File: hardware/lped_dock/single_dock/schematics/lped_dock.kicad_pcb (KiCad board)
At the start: 2 copper layers, 25 x 16 mm, 18 parts, among them J1 V_{OUT}, J2 CONN, J3 GND, J7 USB-C connector, U1 TPD4E02B04DQA, U2 TPS560200

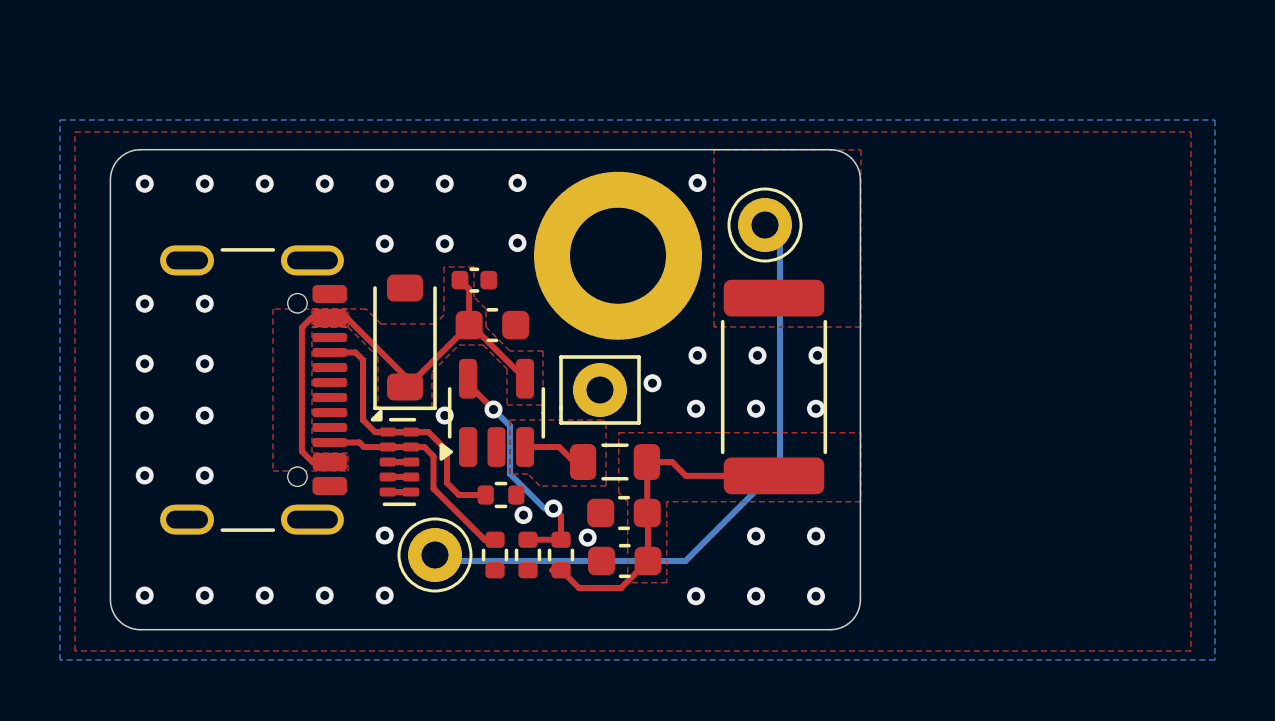
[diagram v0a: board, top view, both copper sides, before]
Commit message: feat(hardware): add battery charger and connector to single charger
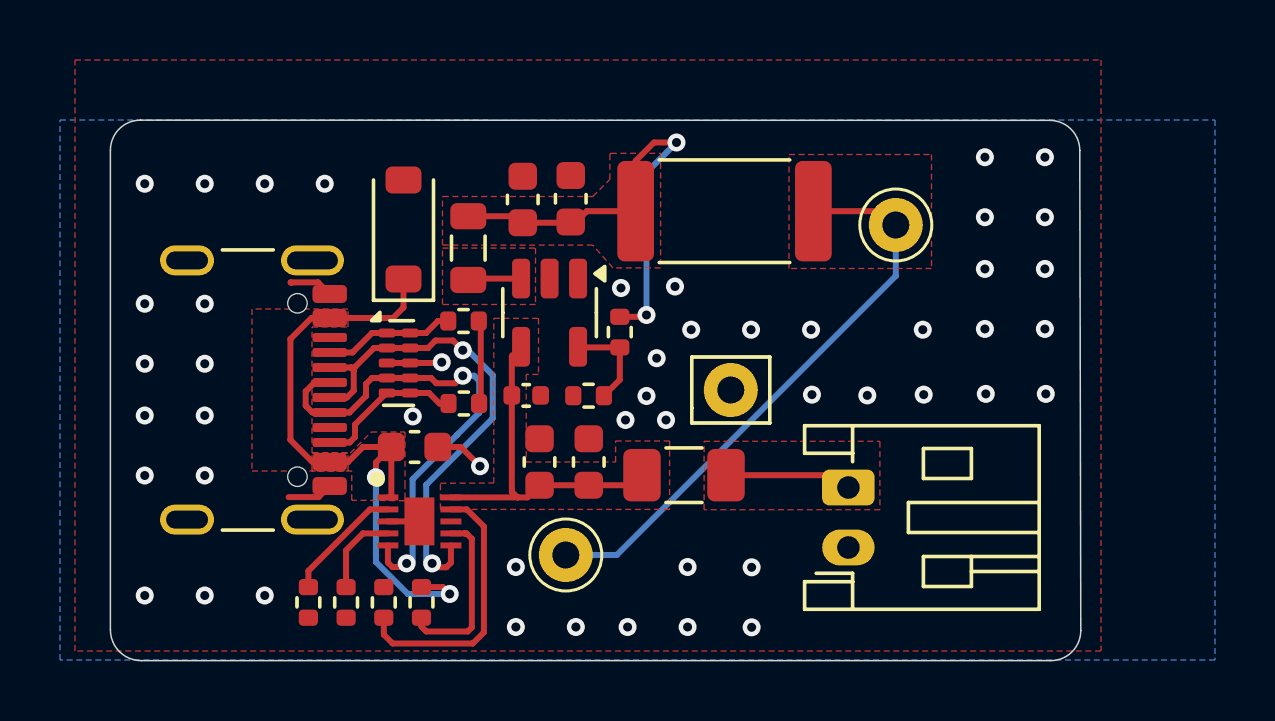
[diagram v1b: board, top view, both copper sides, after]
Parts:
- removed H1: M3, MountingHole:MountingHole_3.2mm_M3_DIN965_Pad
- added BT1: Battery_Cell, Connector_JST:JST_PH_S2B-PH-K_1x02_P2.00mm_Horizontal, F.Cu at (127.3, 112.2)
- added C5: 1u, Capacitor_SMD:C_0603_1608Metric, F.Cu at (112.8, 108.9)
- added C6: 1u, Capacitor_SMD:C_0603_1608Metric, F.Cu at (117.0, 109.4)
- added F1: Polyfuse_Small, Fuse:Fuse_1206_3216Metric, F.Cu at (121.8, 109.8)
- added IC1: BQ24050DSQR, Battery_Chargers:SON40P200X200X80-11N, F.Cu at (113.0, 111.4)
- added R1: 2k7, Resistor_SMD:R_0402_1005Metric, F.Cu at (109.3, 114.1)
- added R7: 10k, Resistor_SMD:R_0402_1005Metric, F.Cu at (113.0, 114.1)
- added R8: 2k, Resistor_SMD:R_0402_1005Metric, F.Cu at (110.5, 114.1)
- added TH1: 10k, Resistor_SMD:R_0402_1005Metric, F.Cu at (111.8, 114.1)
- moved C2 12.5 mm to (116.4, 100.7), turned to 90 degrees
- moved C1 10.6 mm to (118.0, 100.6), turned to 90 degrees
- moved L1 8.65 mm to (114.6, 102.3), turned to 90 degrees
- moved R3 7.68 mm to (119.7, 105.1), turned to -90 degrees
- moved R2 6.09 mm to (123.2, 101.0), turned to 0 degrees
- moved R5 5.93 mm to (114.5, 104.7)
- moved R4 5.68 mm to (118.6, 107.2), turned to 180 degrees
- moved C3 5.58 mm to (118.6, 109.4), turned to 90 degrees
- moved R6 5.16 mm to (114.5, 107.5), turned to 0 degrees
- moved J1 4.36 mm to (128.9, 101.5)
- moved J2 4.36 mm to (117.9, 112.5)
- moved J3 4.36 mm to (123.4, 107.0)
- moved C4 4.21 mm to (116.5, 107.2)
- moved U2 3.78 mm to (117.3, 104.4), turned to -90 degrees
- moved D3 3.60 mm to (112.5, 101.7)
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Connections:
- C3 pad 1: /Regulator/V_{IN} -> /Battery Charger/V_{SYS}
- C4 pad 1: /Regulator/V_{IN} -> /Battery Charger/V_{SYS}
- D3 pad 1: /Regulator/V_{IN} -> /Battery Charger/V_{BUS}
- J7 pad A4: /Regulator/V_{IN} -> /Battery Charger/V_{BUS}
- J7 pad A6: unconnected-(J7-D+-PadA6) -> /USB/USB_D+
- J7 pad A7: unconnected-(J7-D--PadA7) -> /USB/USB_D-
- J7 pad A9: /Regulator/V_{IN} -> /Battery Charger/V_{BUS}
- J7 pad B4: /Regulator/V_{IN} -> /Battery Charger/V_{BUS}
- J7 pad B6: unconnected-(J7-D+-PadB6) -> /USB/USB_D+
- J7 pad B7: unconnected-(J7-D--PadB7) -> /USB/USB_D-
- J7 pad B9: /Regulator/V_{IN} -> /Battery Charger/V_{BUS}
- U1 pad 2: /USB/CC2 -> /USB/USB_D-
- U1 pad 4: /USB/D- -> /USB/USB_D+
- U1 pad 5: /USB/D+ -> /USB/CC2
- U1 pad 6: /USB/D+ -> /USB/CC2
- U1 pad 7: /USB/D- -> /USB/USB_D+
- U1 pad 9: /USB/CC2 -> /USB/USB_D-
- U2 pad 4: /Regulator/V_{IN} -> /Battery Charger/V_{SYS}
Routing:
- net /Battery Charger/V_{BUS}: track 0.00 -> 22.1 mm, vias 0 -> 2
- net /Regulator/V_{IN}: track 16.9 -> 0.00 mm
- net /USB/USB_D+: track 0.00 -> 16.7 mm, vias 0 -> 2
- net /USB/USB_D-: track 0.00 -> 16.7 mm, vias 0 -> 2
- net /Battery Charger/V_{SYS}: track 0.00 -> 11.9 mm
- net Earth: track 1.22 -> 10.4 mm, vias 40 -> 49
- net Net-(IC1-TS): track 0.00 -> 9.04 mm
- net Net-(IC1-ISET2): track 0.00 -> 5.83 mm
- net Net-(C1-Pad1): track 11.6 -> 16.6 mm, vias 0 -> 2
- net /USB/CC1: track 8.97 -> 4.38 mm
- net Net-(U2-FB): track 7.62 -> 3.23 mm, vias 2 -> 0
- net Net-(BT1-+): track 0.00 -> 4.25 mm
- net Net-(IC1-ISET): track 0.00 -> 4.04 mm
- net Net-(IC1-PRETERM): track 0.00 -> 2.85 mm
- net 3V6: track 22.1 -> 19.5 mm
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- added copper zone on F.Cu, net /Battery Charger/V_{BUS}
- added copper zone on F.Cu, net /Battery Charger/V_{SYS}
- added copper zone on F.Cu, net Net-(BT1-+)
- removed copper zone on F.Cu, net /Regulator/V_{IN}
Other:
- board size 25 x 16 mm -> 32.3 x 18 mm
- board text added: "BAT+"
- board text added: "BAT-"

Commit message: feat(hardware): change regulator, add mounting hole to single charger
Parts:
- removed C2: 10u, Capacitor_SMD:C_0603_1608Metric
- removed C4: 0u1, Capacitor_SMD:C_0402_1005Metric
- removed U2: TPS560200, Package_TO_SOT_SMD:SOT-23-5
- added H1: MountingHole, MountingHole:MountingHole_3.2mm_M3, F.Cu at (123.0, 101.5)
- added U3: TLV62080DSGx, Package_SON:WSON-8-1EP_2x2mm_P0.5mm_EP0.9x1.6mm, F.Cu at (118.0, 106.2)
- L1: value 10u -> 1u; footprint Inductor_SMD:L_0805_2012Metric -> Inductor_SMD:L_1008_2520Metric
- R3: value 77k -> 51k
- R4: value 22k -> 36k
- moved R2 9.51 mm to (132.5, 102.8), turned to 90 degrees
- moved R4 7.21 mm to (117.3, 100.1), turned to -90 degrees
- moved C1 6.10 mm to (120.2, 106.3), turned to -90 degrees
- moved R3 5.09 mm to (118.5, 100.1), turned to 90 degrees
- moved L1 2.53 mm to (117.1, 102.7), turned to 0 degrees
- moved R5 1.61 mm to (114.3, 103.1), turned to 90 degrees
- moved C6 0.30 mm to (116.7, 109.5), turned to -90 degrees
- moved C3 0.18 mm to (118.5, 109.5), turned to -90 degrees
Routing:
- net Net-(U3-FB): track 3.23 -> 14.6 mm, vias 0 -> 2
- net /Battery Charger/V_{SYS}: track 11.9 -> 0.57 mm
- net Earth: track 10.4 -> 5.98 mm, vias 49 -> 40
- net Net-(U3-VOS): track 16.6 -> 13.0 mm, vias 2 -> 0
- net 3V6: track 19.5 -> 17.2 mm
- net Net-(U3-SW): track 1.78 -> 0.00 mm
- net /USB/CC1: track 4.38 -> 5.42 mm

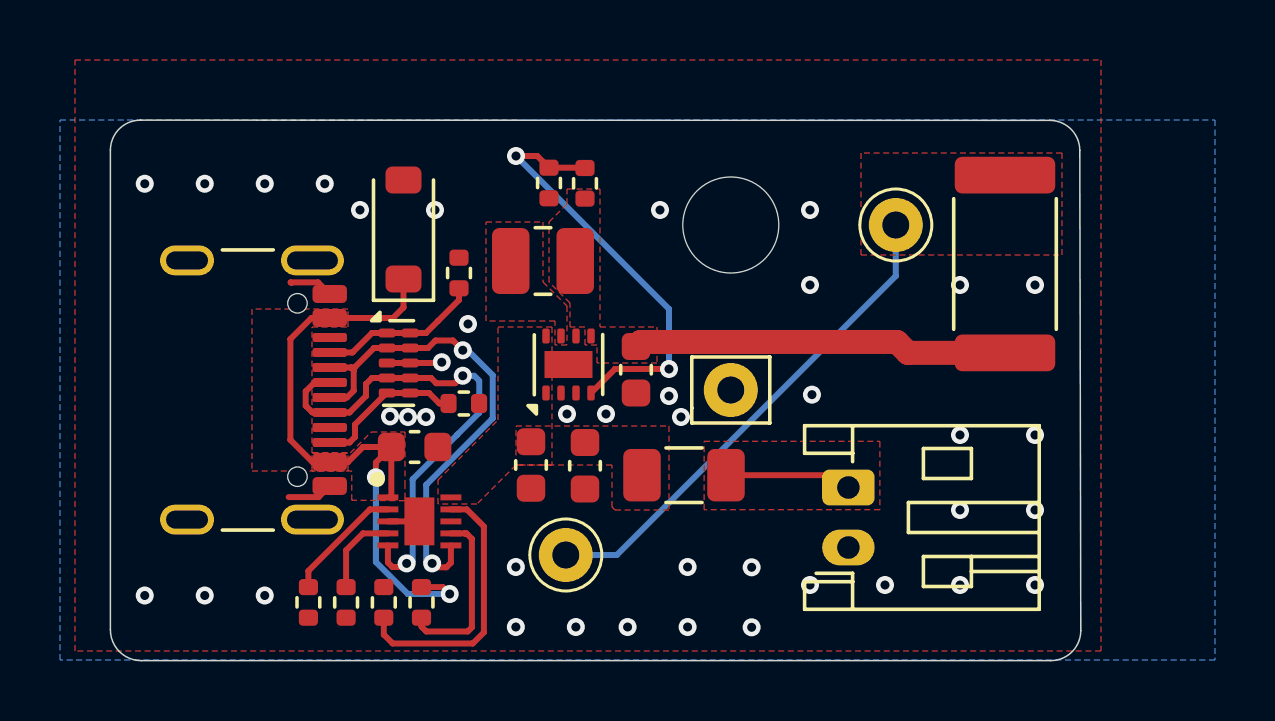
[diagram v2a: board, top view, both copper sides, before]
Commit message: feat(hardware): improvements to dock battery system
* Added current limiting resistor to battery
* Added charging status LED
* Changed side of battery connector
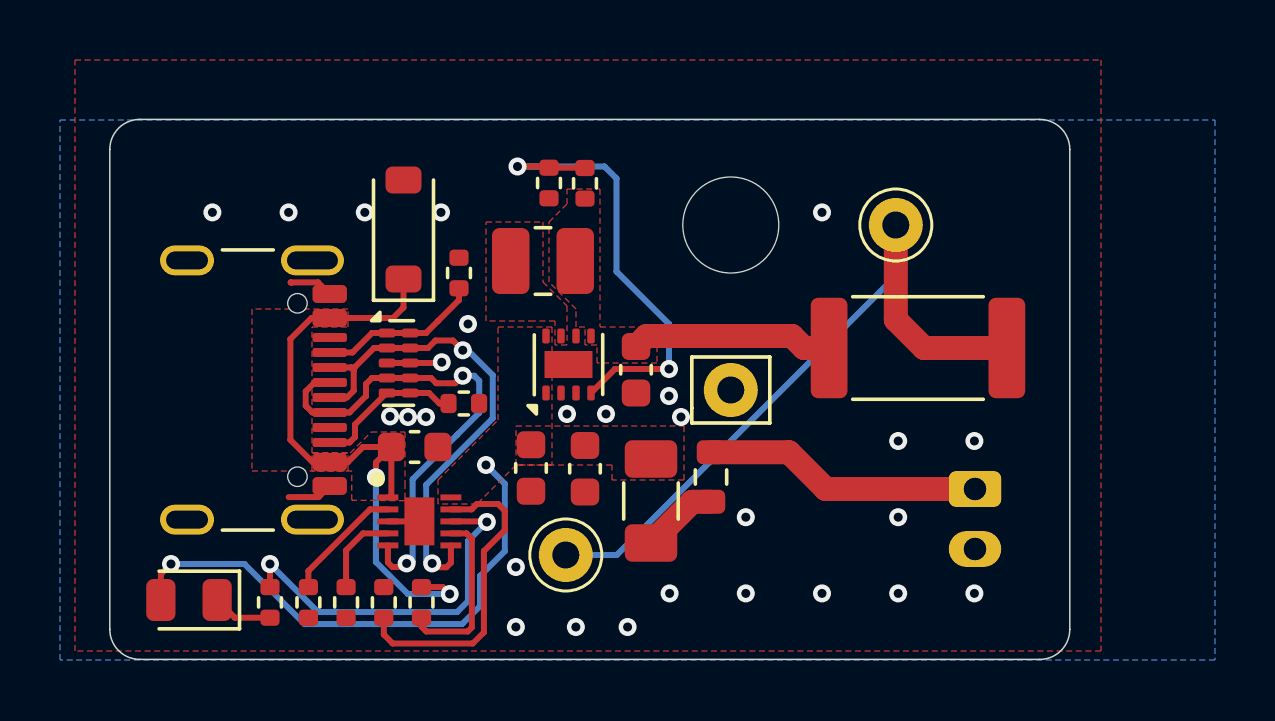
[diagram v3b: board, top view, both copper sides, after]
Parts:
- added D1: CHG, LED_SMD:LED_0805_2012Metric, F.Cu at (105.3, 114.0)
- added R10: 18R, Resistor_SMD:R_0603_1608Metric, F.Cu at (122.7, 109.9)
- added R9: 2k, Resistor_SMD:R_0402_1005Metric, F.Cu at (108.0, 114.1)
- BT1: moved to B.Cu
- F1: value Polyfuse_Small -> 75mA hold
- moved BT1 4.22 mm to (131.5, 112.3)
- moved R2 4.03 mm to (129.6, 105.6), turned to 0 degrees
- moved F1 1.40 mm to (120.7, 110.7), turned to -90 degrees
- moved C3 0.10 mm to (118.5, 109.6)
- moved C6 0.10 mm to (116.7, 109.6)
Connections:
- F1 pad 2: Net-(BT1-+) -> Net-(F1-Pad2)
- IC1 pad 8: unconnected-(IC1-~{CHG}-Pad8) -> Net-(IC1-~{CHG})
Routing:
- net /Battery Charger/V_{SYS}: track 0.57 -> 18.1 mm, vias 0 -> 2
- net Net-(IC1-~{CHG}): track 0.00 -> 12.3 mm, vias 0 -> 2
- net 3V6: track 17.2 -> 24.8 mm
- net Net-(U3-VOS): track 13.0 -> 6.89 mm
- net Net-(BT1-+): track 4.25 -> 9.31 mm
- net Net-(F1-Pad2): track 0.00 -> 2.57 mm
- net Net-(D1-K): track 0.00 -> 2.01 mm
- net Net-(IC1-TS): track 9.04 -> 10.5 mm
- net Net-(U3-FB): track 14.6 -> 15.7 mm
- net Earth: vias 40 -> 27
- removed copper zone on F.Cu, net 3V6
- removed copper zone on F.Cu, net Net-(BT1-+)
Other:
- board size 32.3 x 18 mm -> 32 x 18 mm

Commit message: feat(hardware): add batt charger bypass solder jump
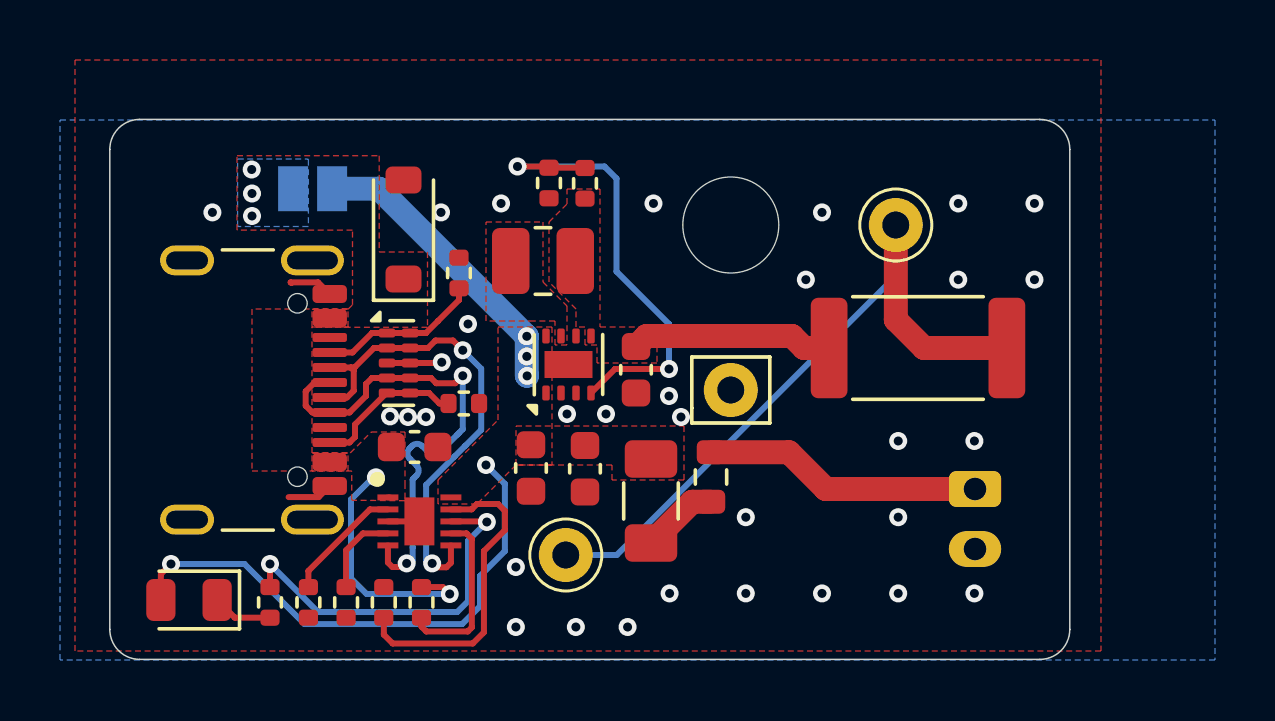
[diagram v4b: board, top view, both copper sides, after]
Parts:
- added JP1: BCH_BYPASS, Jumper:SolderJumper-2_P1.3mm_Open_Pad1.0x1.5mm, B.Cu at (109.4, 100.3)
- BT1: value Battery_Cell -> GeB 331619 75mAh
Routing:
- net /Battery Charger/V_{BUS}: track 22.1 -> 8.71 mm, vias 2 -> 5
- net /Battery Charger/V_{SYS}: track 18.1 -> 27.9 mm, vias 2 -> 5
- net Earth: vias 27 -> 32
- added copper zone on B.Cu, net /Battery Charger/V_{BUS}
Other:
- board text added: "CHGEN"
